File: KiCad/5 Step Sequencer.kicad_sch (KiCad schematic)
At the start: 61 parts, among them J1 RESET IN, J2 TRIG IN, J4 CV OUT, J5 TRIG OUT, Q1 2SA1015, SW1 SW_DPST_x2, SW2 SW_DPST_x2, SW3 SW_DPST_x2, SW4 SW_DPST_x2, SW5 SW_DPST_x2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

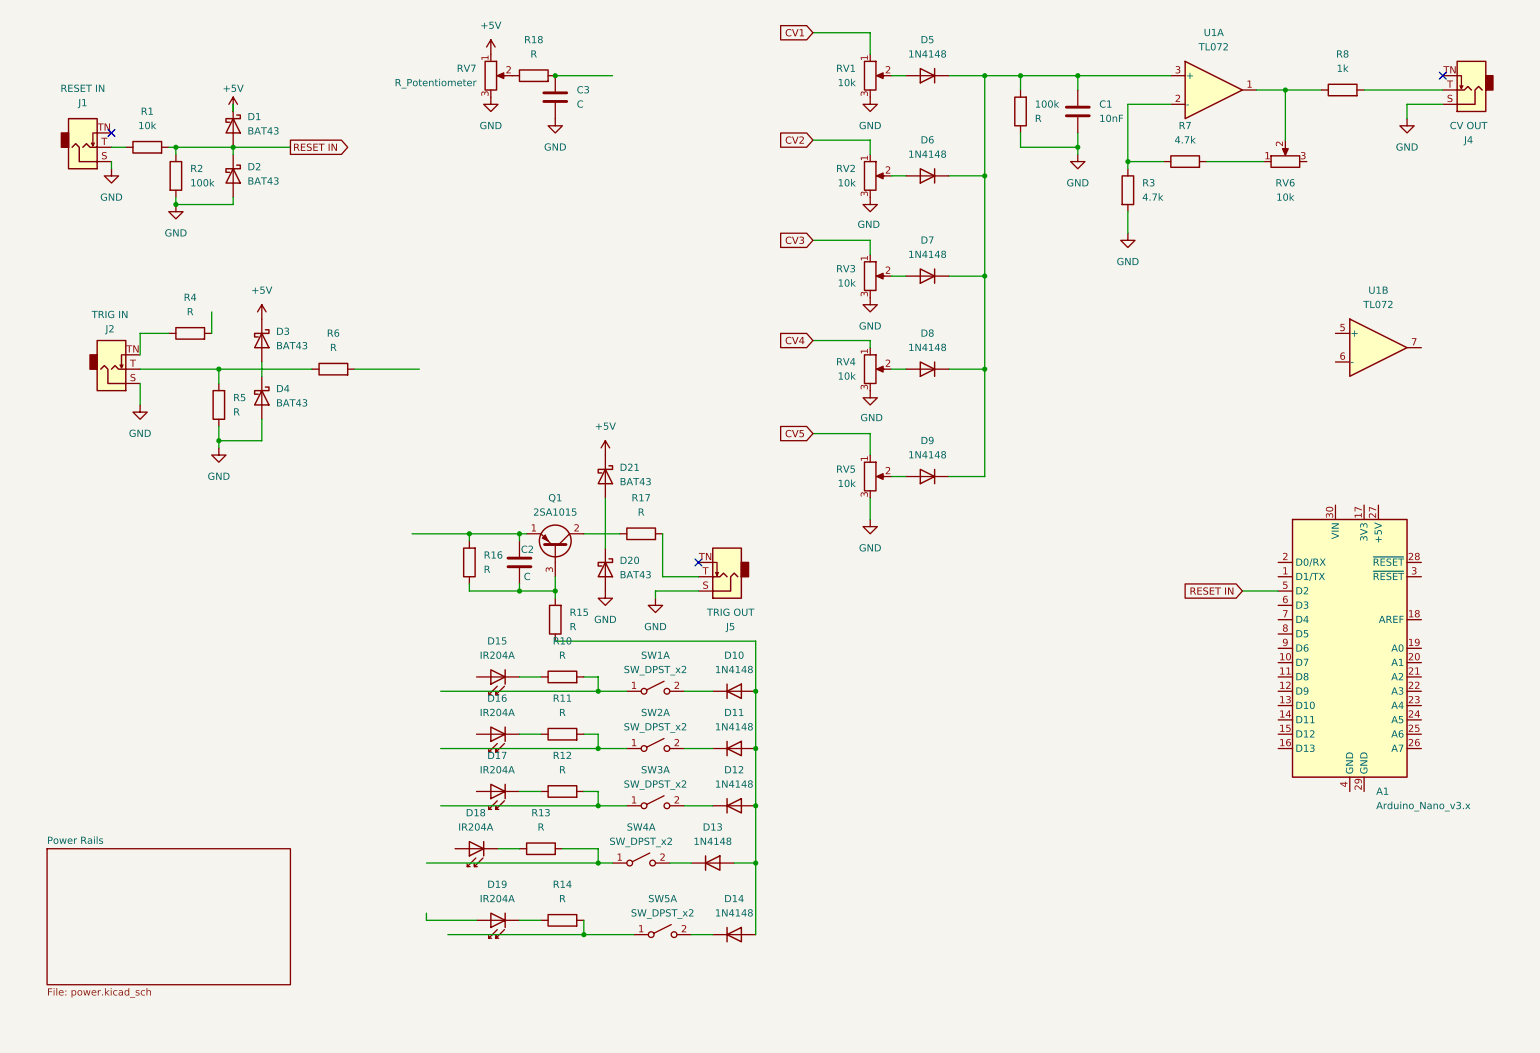
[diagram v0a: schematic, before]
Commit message: feat: rework sequencer switch routing and power sheet
  - add step/output/CV trigger labels and rewired connections
  - replace mode switch with DP3T where needed
  - add power symbols and decoupling parts on the power sheet
  - fix KiCad project metadata and rename the power sheet
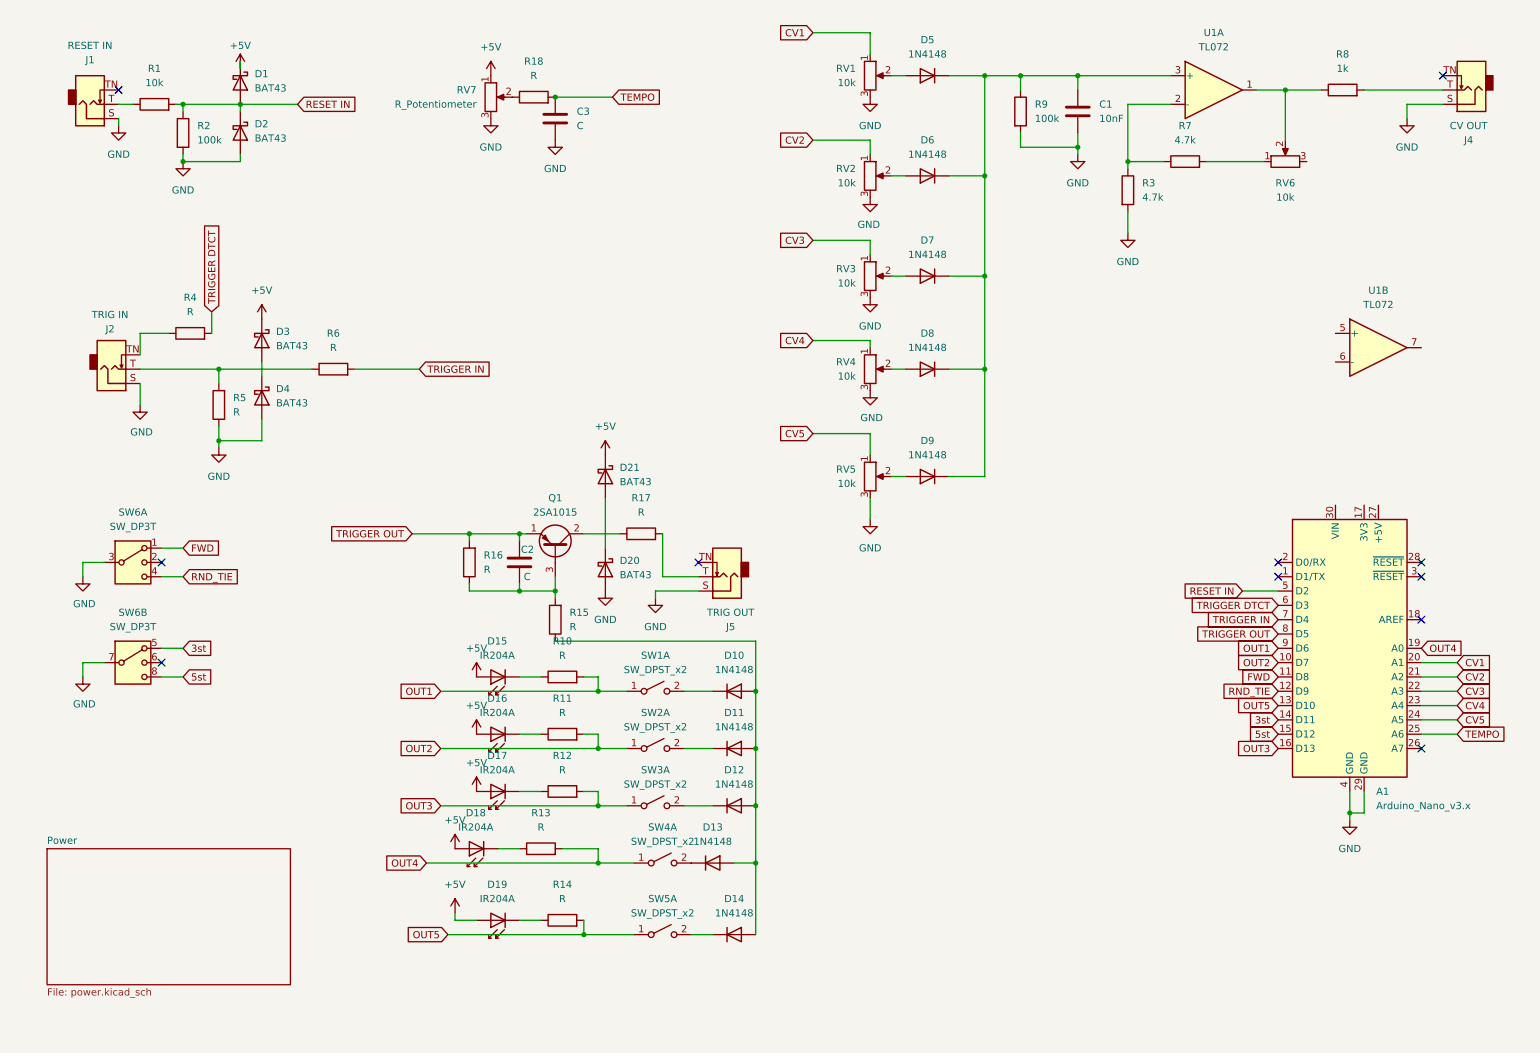
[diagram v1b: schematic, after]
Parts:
- removed 100k: R, symbol Device:R
- added R9: 100k, symbol Device:R
- added SW6: SW_DP3T, symbol Switch:SW_DP3T
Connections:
- net +5V: now also D15.2 (A), D16.2 (A), D17.2 (A), D18.2 (A), D19.2 (A)
- net CV1: now also A1.20 (A1)
- net CV2: now also A1.21 (A2)
- net CV3: now also A1.22 (A3)
- net CV4: now also A1.23 (A4)
- net CV5: now also A1.24 (A5)
- net GND: now also A1.29 (GND), A1.4 (GND), R9.2, SW6.3, SW6.7
- net OUT2: now reaches R11.2, SW2.1 (A)
- net OUT2: now also A1.10 (D7)
- net at C1.1, D5.1 (K), D6.1 (K)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: now also R9.1
- net TRIGGER DTCT: now reaches R4.2
- net TRIGGER DTCT: now also A1.6 (D3)
- net OUT5: now reaches R14.2, SW5.1 (A)
- net OUT5: now also A1.13 (D10)
- net OUT1: now reaches R10.2, SW1.1 (A)
- net OUT1: now also A1.9 (D6)
- net OUT3: now reaches R12.2, SW3.1 (A)
- net OUT3: now also A1.16 (D13)
- net TRIGGER OUT: now reaches C2.1, Q1.1 (E), R16.2
- net TRIGGER OUT: now also A1.8 (D5)
- net TEMPO: now reaches C3.1, R18.2
- net TEMPO: now also A1.25 (A6)
- net FWD: now reaches A1.11 (D8)
- net FWD: now also SW6.1
- net RND_TIE: now reaches A1.12 (D9)
- net RND_TIE: now also SW6.4
- net 3st: now reaches A1.14 (D11)
- net 3st: now also SW6.5
- net 5st: now reaches A1.15 (D12)
- net 5st: now also SW6.8
- net OUT4: now reaches A1.19 (A0)
- net OUT4: now also R13.2, SW4.1 (A)
- net TRIGGER IN: now reaches A1.7 (D4)
- net TRIGGER IN: now also R6.2
- no-connect marks 3 -> 11
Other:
- sheet Power Rails renamed Power
- moved on the sheet: C3, D1, D2, J1, R1, R18, R2, RV7

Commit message: feat(kicad): add +5V bulk decoupling and tidy schematic layout
  - add C13 as a 10uF polarized capacitor across +5V and GND
  - add project title/revision metadata and clearer section labels
  - rename the power sheet to "EURORACK POWER"
  - clean up power-sheet wiring, grounding, and text placement
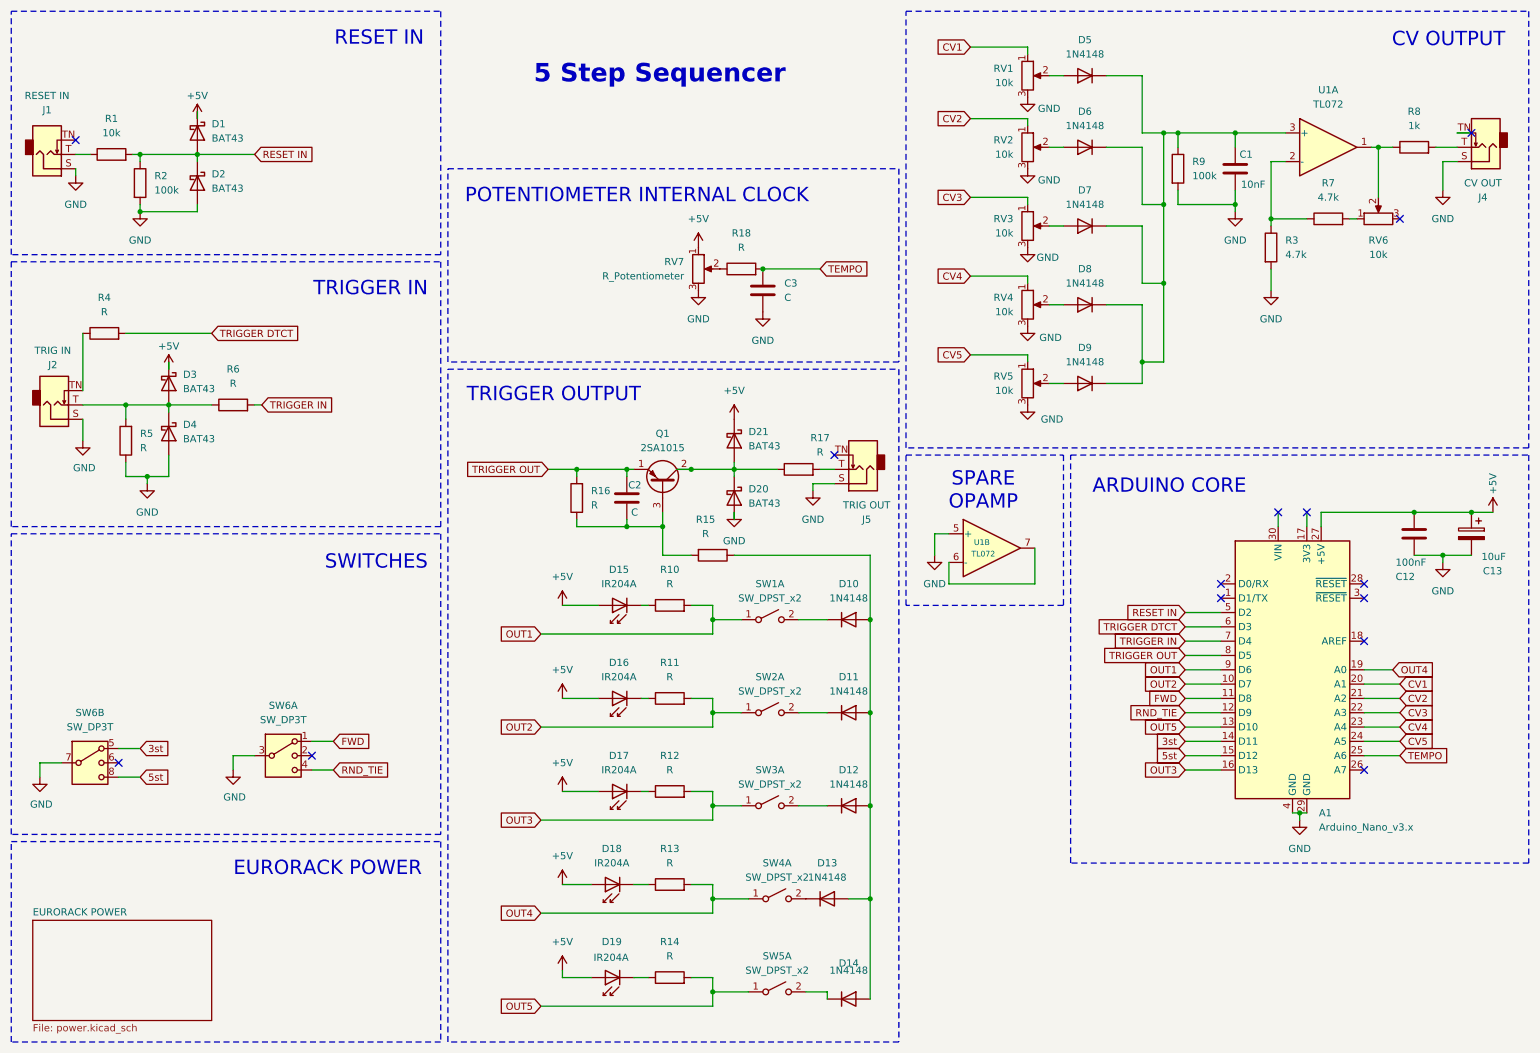
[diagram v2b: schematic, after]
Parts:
- added C12: 100nF, Capacitor_SMD:C_0805_2012Metric_Pad1.18x1.45mm_HandSolder, symbol Device:C
- added C13: 10uF, Capacitor_SMD:CP_Elec_5x5.4, symbol Device:C_Polarized
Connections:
- net +5V: now also A1.27 (+5V), C12.1, C13.1
- net GND: now also U1.5 (+), C12.2, C13.2
- net at Q1.2 (C), R17.1: now also D20.1 (K), D21.2 (A)
- net at U1.6 (-): now also U1.7
- net at J2.T, R5.2, R6.1: now also D3.2 (A), D4.1 (K)
- no-connect marks 11 -> 14
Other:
- sheet Power renamed EURORACK POWER
- note added: "5 Step Sequencer"
- note added: "ARDUINO CORE"
- note added: "CV OUTPUT"
- note added: "EURORACK POWER"
- note added: "POTENTIOMETER INTERNAL CLOCK"
- note added: "RESET IN"
- note added: "SPARE OPAMP"
- note added: "SWITCHES"
- note added: "TRIGGER IN"
- note added: "TRIGGER OUTPUT"
- company: (none) -> Dirty Dream - Nathanael Noir
- title: (none) -> 5 Step Sequencer
- moved on the sheet: A1, C1, C2, C3, D1, D10, D11, D12, D13, D14, D15, D16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

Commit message: chore(kicad): annotate component values and tidy step-stage wiring
  - replace placeholder resistor, capacitor, and potentiometer values with real part values
  - clean up wire connections around the D10-D14 step-stage diode network
  - adjust symbol and label placement to match the updated routing
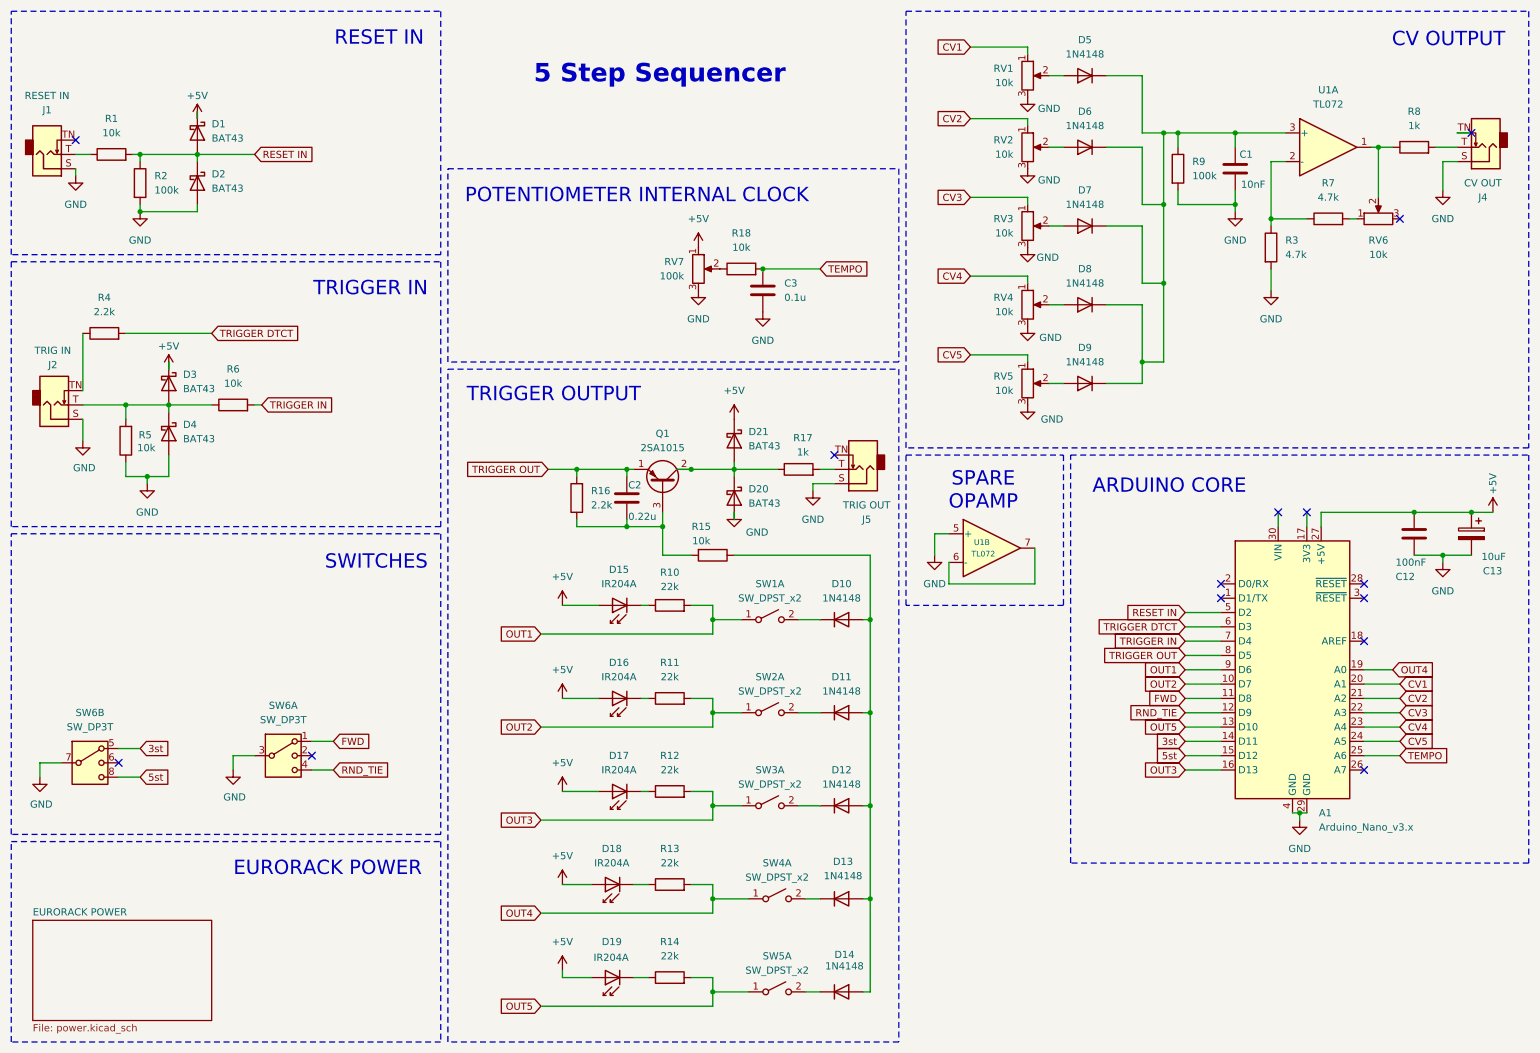
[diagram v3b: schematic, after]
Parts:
- C2: value C -> 0.22u
- C3: value C -> 0.1u
- R10, R11, R12, R13, R14: value R -> 22k
- R15, R18, R5, R6: value R -> 10k
- R16, R4: value R -> 2.2k
- R17: value R -> 1k
- RV7: value R_Potentiometer -> 100k
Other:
- moved on the sheet: D10, D11, D12, D13, D14

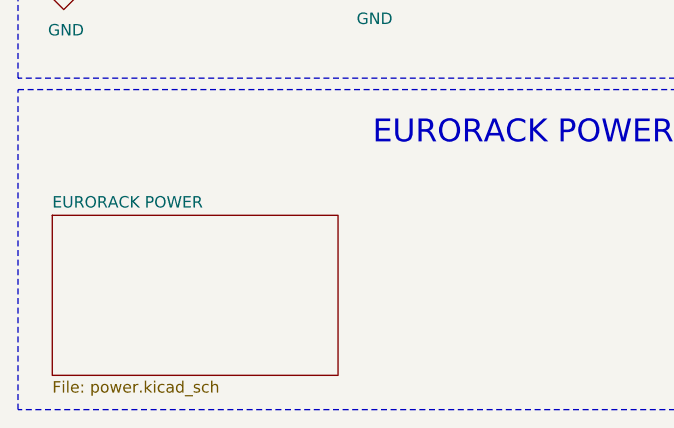
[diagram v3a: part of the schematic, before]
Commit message: Changing Sheet Names
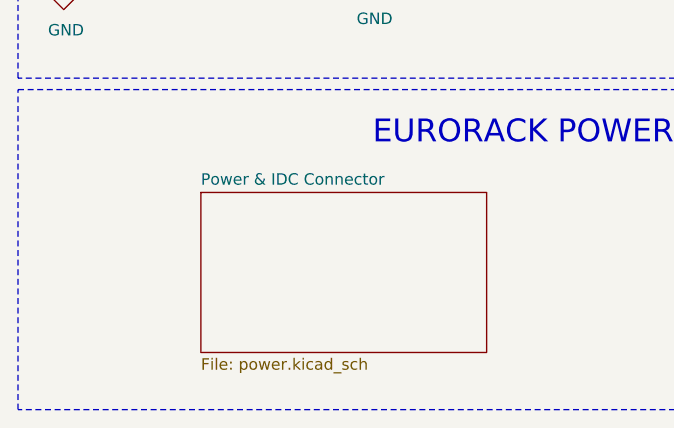
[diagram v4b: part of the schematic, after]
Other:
- sheet EURORACK POWER renamed Power & IDC Connector
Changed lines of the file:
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@@
 	)
 	(sheet
-		(at 17.78 175.26)
+		(at 34.29 172.72)
 		(size 31.75 17.78)
 		(exclude_from_sim no)
@@
 			(color 0 0 0 0.0000)
 		)
-		(property "Sheetname" "EURORACK POWER"
-			(at 17.78 174.5484 0)
+		(property "Sheetname" "Power & IDC Connector"
+			(at 34.29 172.0084 0)
 			(effects
 				(font
@@
 		)
 		(property "Sheetfile" "power.kicad_sch"
-			(at 17.78 193.6246 0)
+			(at 34.29 191.0846 0)
 			(effects
 				(font
